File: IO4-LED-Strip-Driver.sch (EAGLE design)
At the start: 21 parts, among them Q1 DMN4468, Q2 DMN4468, Q3 DMN4468, Q7 DMN4468

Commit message: version#
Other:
- note added: "1.0"
- note added: "Drives 2x RGB strips and 2x White strips with a 12v/15A power supply (For backdrop and valence controlled lighting)"
- note removed: "2.0b"
- note removed: "Drives 2x RGB strips and 2x White strips with a 12v/15A power supply (For backdrop and valence controlled lighting) v2.0b: default address=0, silkscreen changes"
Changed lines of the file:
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@@
 <text x="149.86" y="25.4" size="3.81" layer="97">IO4 LED Strip Driver</text>
 <text x="152.908" y="6.35" size="3.81" layer="97">John Plocher</text>
-<text x="235.458" y="6.604" size="3.81" layer="97">2.0b</text>
+<text x="235.458" y="6.604" size="3.81" layer="97">1.0</text>
 <text x="147.32" y="38.1" size="1.6764" layer="102">Drives 2x RGB strips and 2x White strips with a 12v/15A power supply
-(For backdrop and valence controlled lighting)
-v2.0b: default address=0, silkscreen changes</text>
+(For backdrop and valence controlled lighting)</text>
 <text x="147.32" y="118.11" size="2.54" layer="91">+
 R

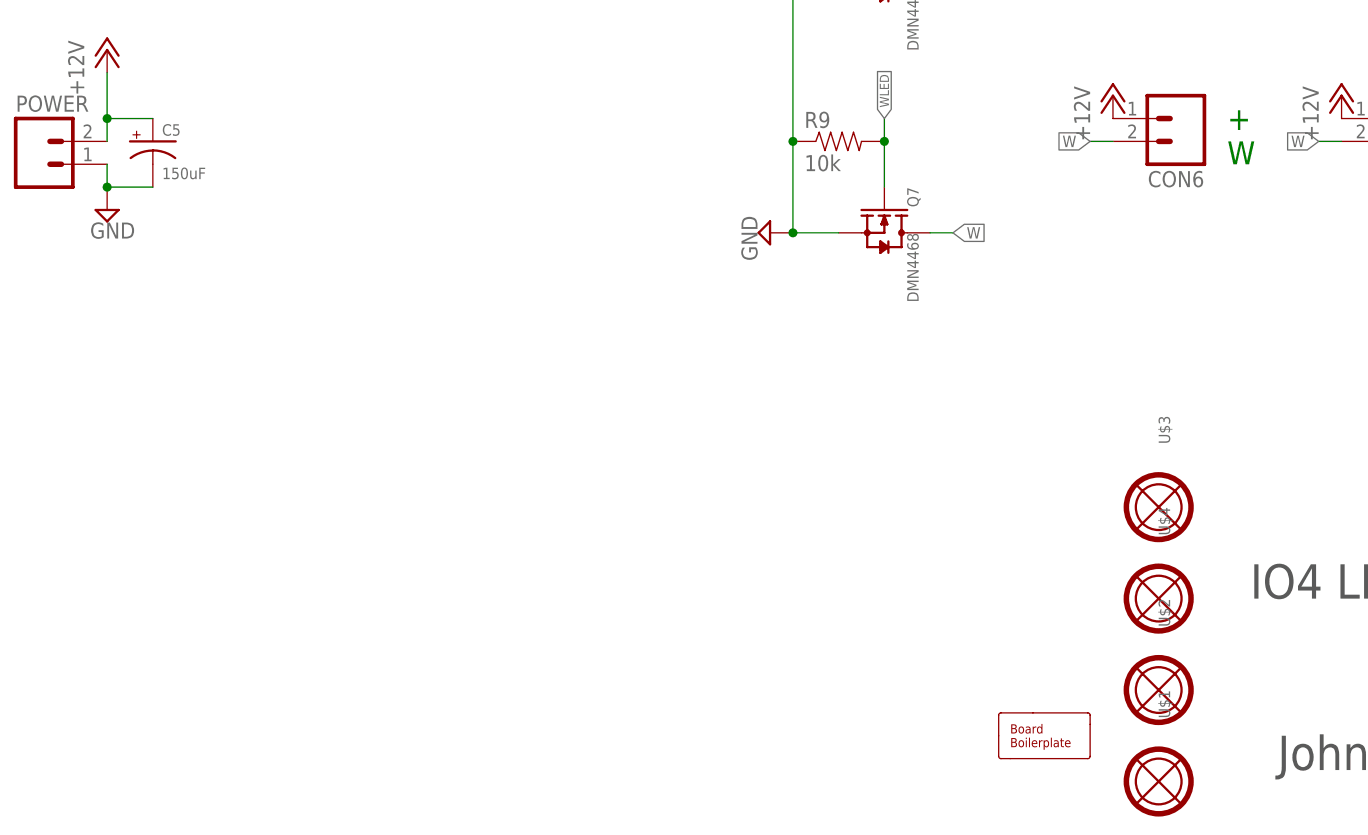
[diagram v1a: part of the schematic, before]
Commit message: silkscreen changes
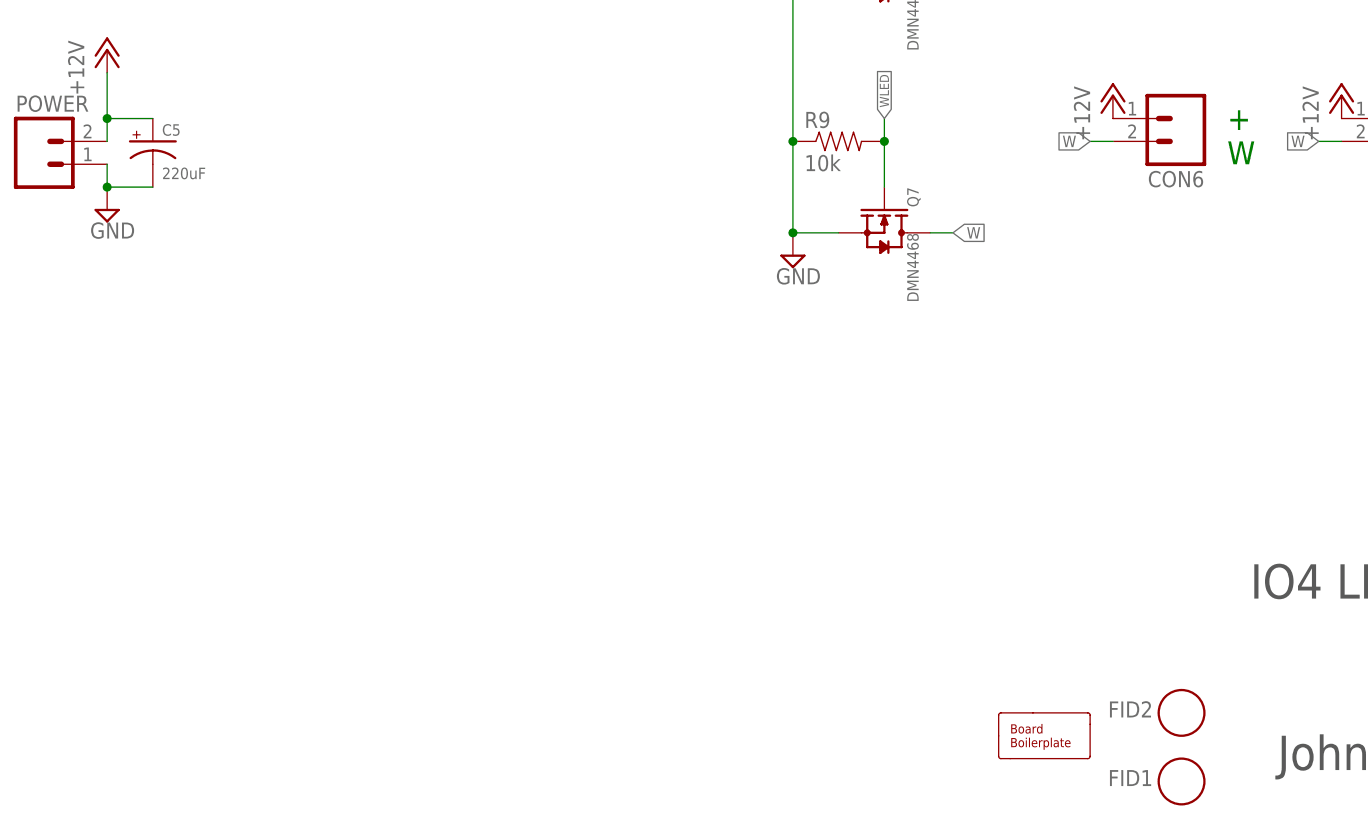
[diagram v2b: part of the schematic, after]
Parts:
- removed U$1, U$2, U$3, U$4: MOUNTINGHOLE, SPCoast:MOUNTINGHOLE
- added FID1, FID2: FIDUCIAL, SPCoast:FIDUCIAL
- BOARD1: value BOARD80X100-TEMPLATE -> BOARD80X100; device SPCoast:BOARD80X100-TEMPLATE -> SPCoast:BOARD80X100
- C5: value 150uF -> 220uF
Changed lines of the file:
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@@
 <layer number="14" name="Route14" color="1" fill="6" visible="no" active="no"/>
 <layer number="15" name="Route15" color="4" fill="6" visible="no" active="no"/>
-<layer number="16" name="Bottom" color="1" fill="1" visible="no" active="no"/>
-<layer number="17" name="Pads" color="2" fill="1" visible="no" active="no"/>
-<layer number="18" name="Vias" color="2" fill="1" visible="no" active="no"/>
+<layer number="16" name="Bottom" color="2" fill="1" visible="no" active="no"/>
+<layer number="17" name="Pads" color="23" fill="1" visible="no" active="no"/>
+<layer number="18" name="Vias" color="29" fill="1" visible="no" active="no"/>
 <layer number="19" name="Unrouted" color="6" fill="1" visible="no" active="no"/>
 <layer number="20" name="Dimension" color="15" fill="1" visible="no" active="no"/>
-<layer number="21" name="tPlace" color="7" fill="1" visible="no" active="no"/>
-<layer number="22" name="bPlace" color="7" fill="1" visible="no" active="no"/>
-<layer number="23" name="tOrigins" color="15" fill="1" visible="no" active="no"/>
+<layer number="21" name="tPlace" color="19" fill="1" visible="no" active="no"/>
+<layer number="22" name="bPlace" color="17" fill="1" visible="no" active="no"/>
+<layer number="23" name="tOrigins" color="30" fill="1" visible="no" active="no"/>
 <layer number="24" name="bOrigins" color="15" fill="1" visible="no" active="no"/>
-<layer number="25" name="tNames" color="7" fill="1" visible="no" active="no"/>
-<layer number="26" name="bNames" color="7" fill="1" visible="no" active="no"/>
-<layer number="27" name="tValues" color="7" fill="1" visible="no" active="no"/>
+<layer number="25" name="tNames" color="63" fill="1" visible="no" active="no"/>
+<layer number="26" name="bNames" color="34" fill="1" visible="no" active="no"/>
+<layer number="27" name="tValues" color="56" fill="1" visible="no" active="no"/>
 <layer number="28" name="bValues" color="7" fill="1" visible="no" active="no"/>
 <layer number="29" name="tStop" color="7" fill="3" visible="no" active="no"/>
@@
 <layer number="38" name="bTest" color="7" fill="1" visible="no" active="no"/>
 <layer number="39" name="tKeepout" color="4" fill="11" visible="no" active="no"/>
-<layer number="40" name="bKeepout" color="1" fill="11" visible="no" active="no"/>
+<layer number="40" name="bKeepout" color="3" fill="11" visible="no" active="no"/>
 <layer number="41" name="tRestrict" color="4" fill="10" visible="no" active="no"/>
-<layer number="42" name="bRestrict" color="1" fill="10" visible="no" active="no"/>
+<layer number="42" name="bRestrict" color="3" fill="10" visible="no" active="no"/>
 <layer number="43" name="vRestrict" color="2" fill="10" visible="no" active="no"/>
-<layer number="44" name="Drills" color="7" fill="1" visible="no" active="no"/>
-<layer number="45" name="Holes" color="7" fill="1" visible="no" active="no"/>
-<layer number="46" name="Milling" color="3" fill="1" visible="no" active="no"/>
-<layer number="47" name="Measures" color="7" fill="1" visible="no" active="no"/>
-<layer number="48" name="Document" color="7" fill="1" visible="no" active="no"/>
-<layer number="49" name="Reference" color="7" fill="1" visible="no" active="no"/>
+<layer number="44" name="Drills" color="16" fill="1" visible="no" active="no"/>
+<layer number="45" name="Holes" color="35" fill="1" visible="no" active="no"/>
+<layer number="46" name="Milling" color="50" fill="1" visible="no" active="no"/>
+<layer number="47" name="Measures" color="21" fill="1" visible="no" active="no"/>
+<layer number="48" name="Document" color="24" fill="1" visible="no" active="no"/>
+<layer number="49" name="Reference" color="48" fill="1" visible="no" active="no"/>
 <layer number="50" name="dxf" color="7" fill="1" visible="no" active="no"/>
-<layer number="51" name="tDocu" color="7" fill="1" visible="no" active="no"/>
+<layer number="51" name="tDocu" color="24" fill="1" visible="no" active="no"/>
 <layer number="52" name="bDocu" color="7" fill="1" visible="no" active="no"/>
 <layer number="53" name="tGND_GNDA" color="7" fill="9" visible="no" active="no"/>
@@
 </classes>
 <parts>
-<part name="BOARD1" library="SPCoast" deviceset="BOARD" device="80X100-TEMPLATE"/>
+<part name="BOARD1" library="SPCoast" deviceset="BOARD" device="80X100" value="BOARD80X100"/>
 <part name="FRAME2" library="MCP" deviceset="FRAME-LETTER" device=""/>
 <part name="OSHW1" library="SparkFun" deviceset="OSHW-LOGO" device="L" value="OSHW-LOGOL"/>
-<part name="C5" library="SPCoast" deviceset="CAP-POL*" device="0810" value="150uF"/>
+<part name="C5" library="SPCoast" deviceset="CAP-POL*" device="0810" value="220uF"/>
 <part name="P+2" library="SPCoast" deviceset="+12V" device=""/>
 <part name="P+4" library="SPCoast" deviceset="+12V" device=""/>
@@
 <part name="CON3" library="SPCoast" deviceset="CONNECTOR-M04" device="5.08"/>
 <part name="POWER" library="SPCoast" deviceset="CONNECTOR-M02" device="MSTBA2"/>
-<part name="U$1" library="SPCoast" deviceset="MOUNTINGHOLE" device=""/>
-<part name="U$2" library="SPCoast" deviceset="MOUNTINGHOLE" device=""/>
-<part name="U$4" library="SPCoast" deviceset="MOUNTINGHOLE" device=""/>
-<part name="U$3" library="SPCoast" deviceset="MOUNTINGHOLE" device=""/>
 <part name="R5" library="SPCoast" deviceset="R*" device="0603-RES" value="10k"/>
 <part name="R3" library="SPCoast" deviceset="R*" device="0603-RES" value="10k"/>
@@
 <part name="P+8" library="SPCoast" deviceset="+12V" device=""/>
 <part name="CON8" library="SPCoast" deviceset="CONNECTOR-M04" device="5.08"/>
+<part name="FID1" library="SPCoast" deviceset="FIDUCIAL" device=""/>
+<part name="FID2" library="SPCoast" deviceset="FIDUCIAL" device=""/>
 </parts>
 <sheets>
@@
 <instance part="Q1" gate="Q" x="109.22" y="93.98" rot="R270"/>
 <instance part="Q7" gate="Q" x="109.22" y="66.04" rot="R270"/>
-<instance part="V29" gate="GND" x="96.52" y="66.04" rot="R270"/>
+<instance part="V29" gate="GND" x="99.06" y="63.5"/>
 <instance part="CON3" gate="J" x="139.7" y="124.46" rot="R180"/>
 <instance part="POWER" gate="J" x="17.78" y="73.66"/>
-<instance part="U$1" gate="MT1" x="139.7" y="5.08" rot="R270"/>
-<instance part="U$2" gate="MT1" x="139.7" y="15.24" rot="R270"/>
-<instance part="U$4" gate="MT1" x="139.7" y="25.4" rot="R270"/>
-<instance part="U$3" gate="MT1" x="139.7" y="35.56" rot="R270"/>
 <instance part="R5" gate="R" x="104.14" y="157.48"/>
 <instance part="R3" gate="R" x="104.14" y="132.08"/>
@@
 <instance part="P+8" gate="1" x="160.02" y="129.54"/>
 <instance part="CON8" gate="J" x="165.1" y="124.46" rot="R180"/>
+<instance part="FID1" gate="FID1" x="142.24" y="5.08"/>
+<instance part="FID2" gate="FID1" x="142.24" y="12.7"/>
 </instances>
 <busses>

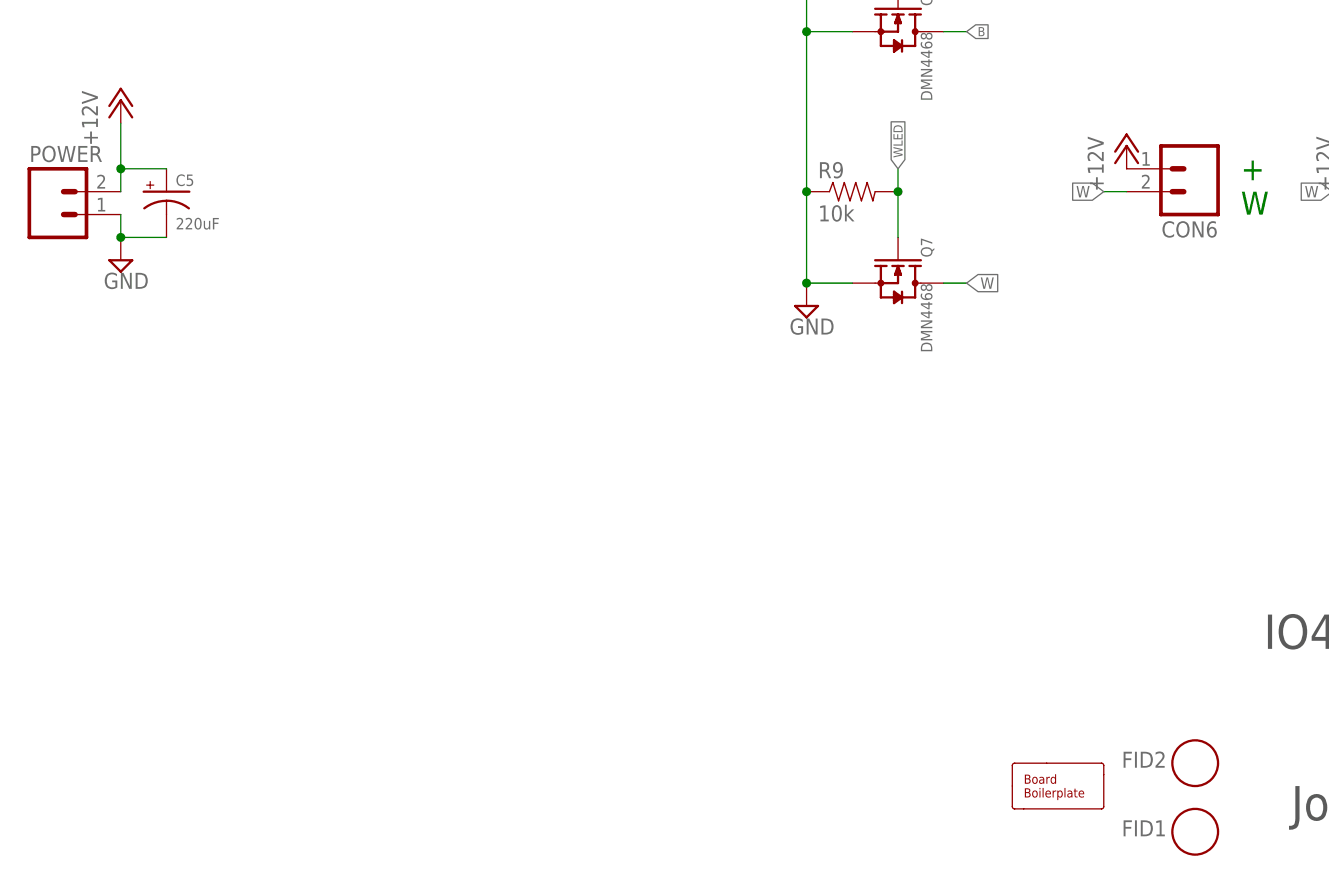
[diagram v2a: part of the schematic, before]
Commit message: FID placement & rerouting
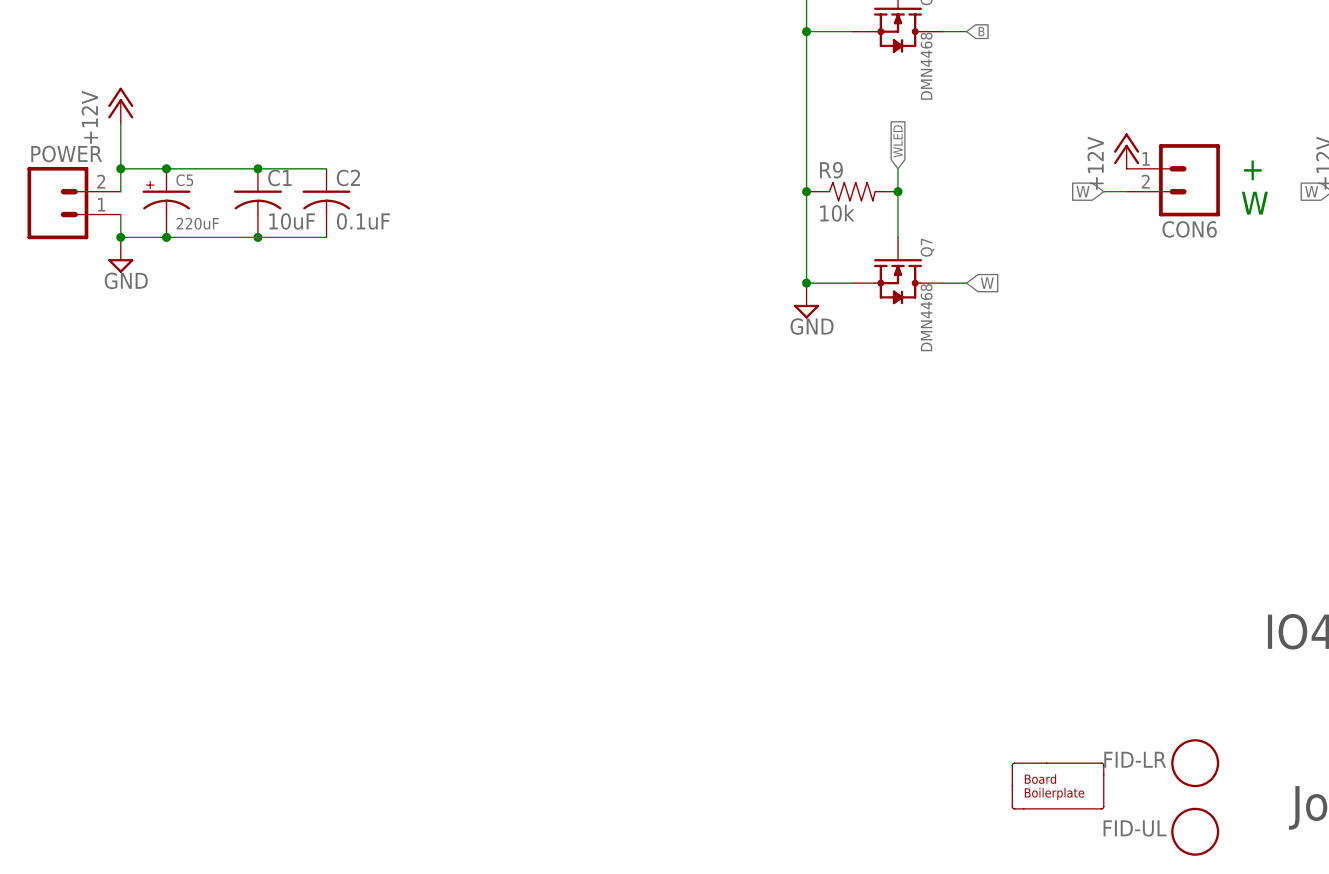
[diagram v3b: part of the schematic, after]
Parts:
- added C1: 10uF, SPCoast:CAP0603
- added C2: 0.1uF, SPCoast:CAP0603
- renumbered FID1 to FID-UL, FID2 to FID-LR
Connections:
- net +12V: now also C1.1, C2.1
- net GND: now also C1.2, C2.2
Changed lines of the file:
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@@
 <part name="P+8" library="SPCoast" deviceset="+12V" device=""/>
 <part name="CON8" library="SPCoast" deviceset="CONNECTOR-M04" device="5.08"/>
-<part name="FID1" library="SPCoast" deviceset="FIDUCIAL" device=""/>
-<part name="FID2" library="SPCoast" deviceset="FIDUCIAL" device=""/>
+<part name="FID-UL" library="SPCoast" deviceset="FIDUCIAL" device=""/>
+<part name="FID-LR" library="SPCoast" deviceset="FIDUCIAL" device=""/>
+<part name="C1" library="SPCoast" deviceset="CAP*" device="0603" value="10uF"/>
+<part name="C2" library="SPCoast" deviceset="CAP*" device="0603" value="0.1uF"/>
 </parts>
 <sheets>
@@
 <instance part="P+8" gate="1" x="160.02" y="129.54"/>
 <instance part="CON8" gate="J" x="165.1" y="124.46" rot="R180"/>
-<instance part="FID1" gate="FID1" x="142.24" y="5.08"/>
-<instance part="FID2" gate="FID1" x="142.24" y="12.7"/>
+<instance part="FID-UL" gate="FID1" x="142.24" y="5.08"/>
+<instance part="FID-LR" gate="FID1" x="142.24" y="12.7"/>
+<instance part="C1" gate="C1" x="38.1" y="76.2"/>
+<instance part="C2" gate="C1" x="45.72" y="76.2"/>
 </instances>
 <busses>
@@
 <pinref part="V2" gate="GND" pin="GND"/>
 <junction x="22.86" y="71.12"/>
+<pinref part="C2" gate="C1" pin="2"/>
+<pinref part="C1" gate="C1" pin="2"/>
+<wire x1="45.72" y1="71.12" x2="38.1" y2="71.12" width="0.1524" layer="91"/>
+<wire x1="38.1" y1="71.12" x2="27.94" y2="71.12" width="0.1524" layer="91"/>
+<junction x="38.1" y="71.12"/>
+<junction x="27.94" y="71.12"/>
 </segment>
 </net>
@@
 <junction x="22.86" y="78.74"/>
 <pinref part="POWER" gate="J" pin="B"/>
+<pinref part="C1" gate="C1" pin="1"/>
+<wire x1="27.94" y1="78.74" x2="38.1" y2="78.74" width="0.1524" layer="91"/>
+<junction x="27.94" y="78.74"/>
+<pinref part="C2" gate="C1" pin="1"/>
+<wire x1="38.1" y1="78.74" x2="45.72" y2="78.74" width="0.1524" layer="91"/>
+<junction x="38.1" y="78.74"/>
 </segment>
 <segment>
